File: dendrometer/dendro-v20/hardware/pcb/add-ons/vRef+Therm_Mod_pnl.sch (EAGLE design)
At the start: 8 parts, among them J1 MF-CON-2.54mm-01x03, J2 CON_01X01LUX, J3 MF-CON-2.54mm-01x03, U1 AAT1217-SOT23-6

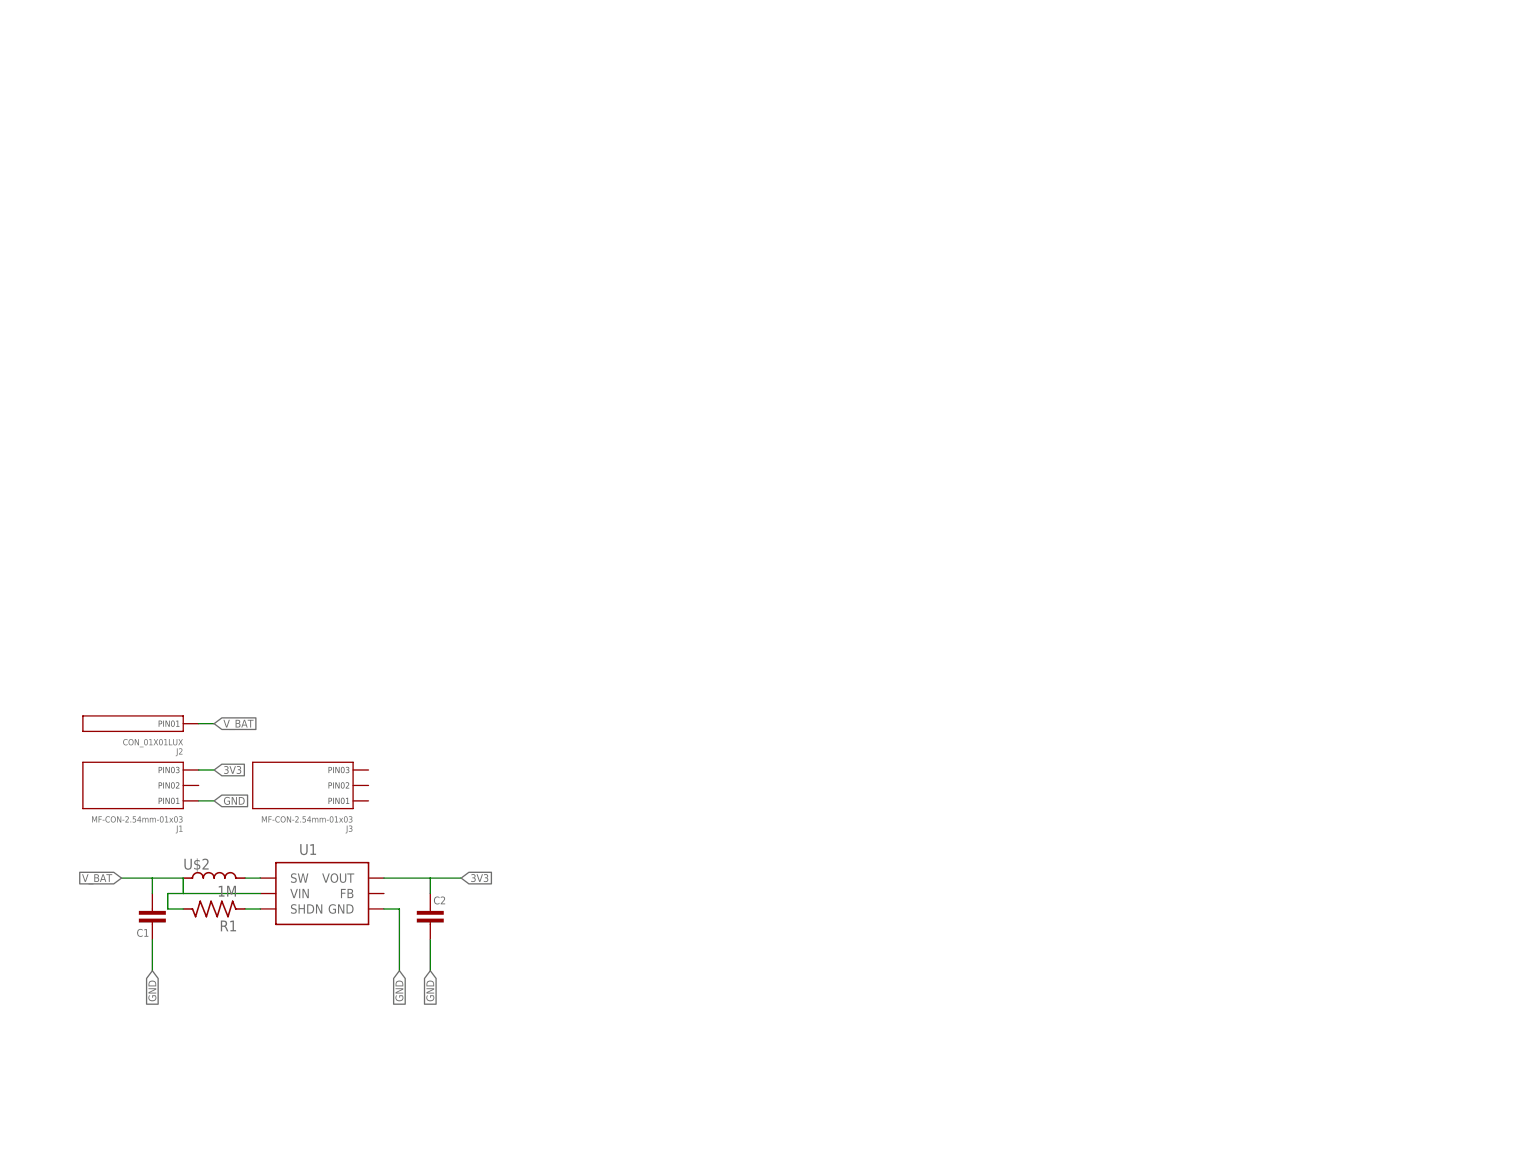
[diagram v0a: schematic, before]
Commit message: making add-on boards for dendro upgrades)
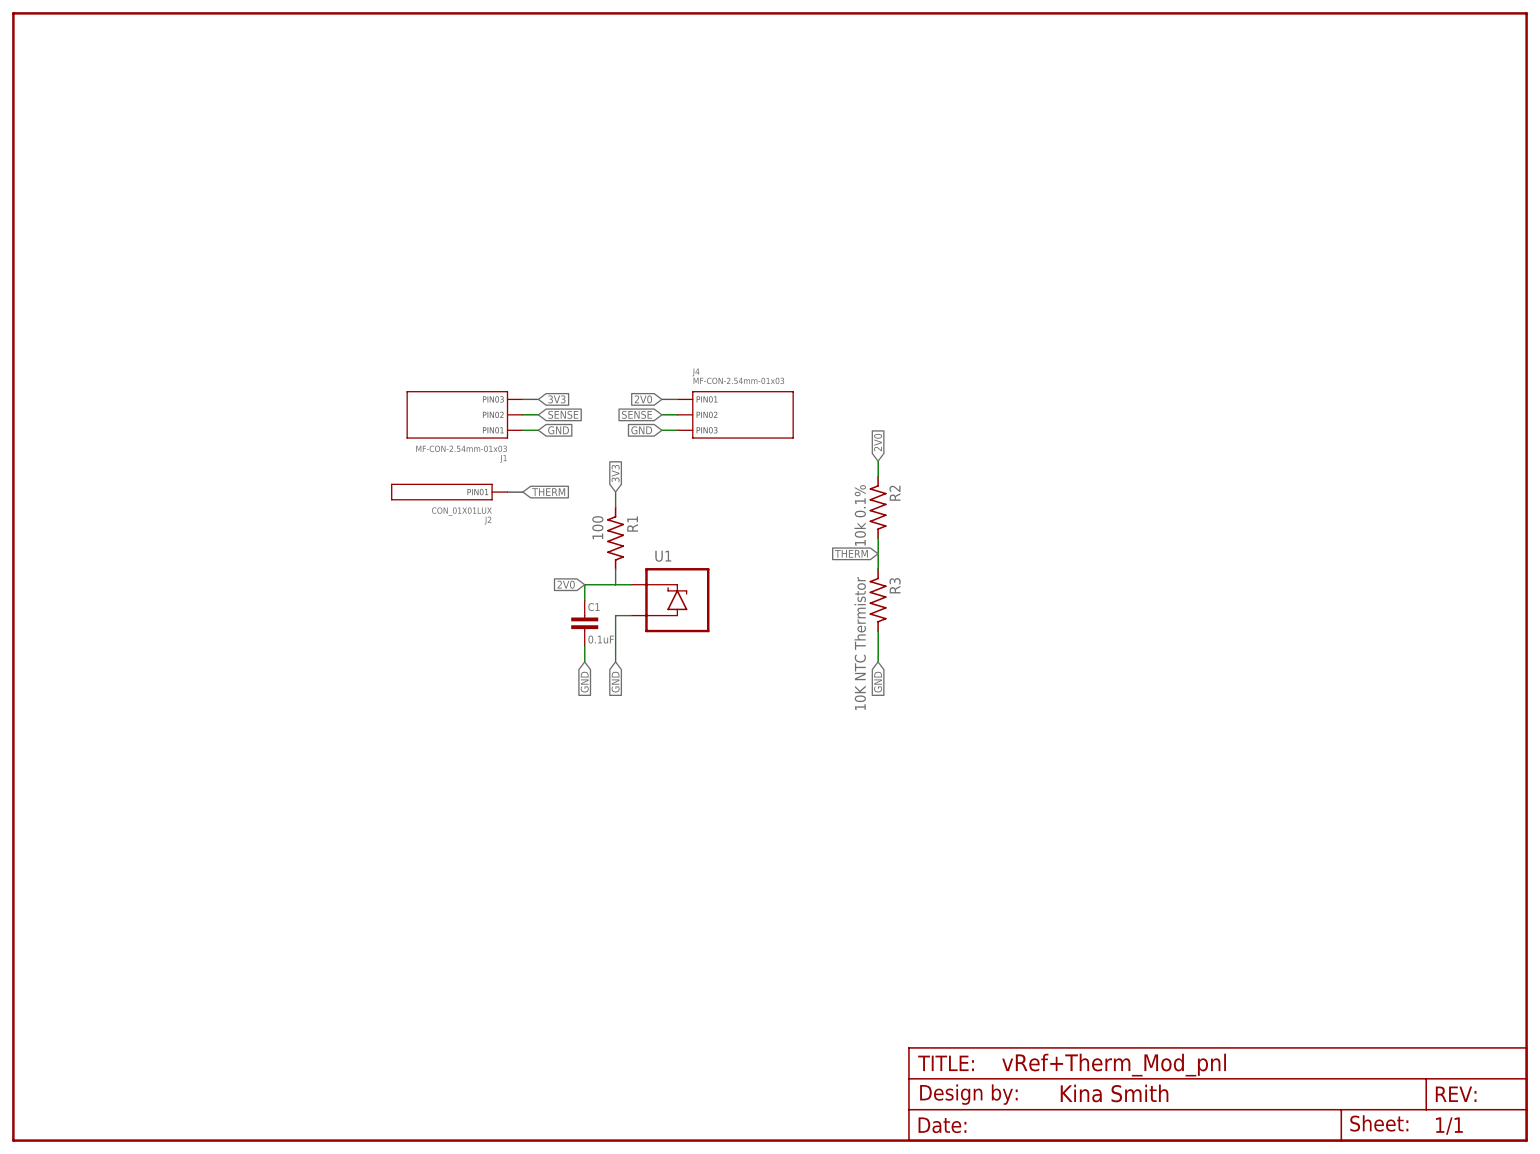
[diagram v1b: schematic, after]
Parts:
- removed C2: (no value), My_Passives:CAPACITOR_NP0603-N
- removed J3: MF-CON-2.54mm-01x03, My_Connectors:CON_01X03_PTH_2.54MM
- removed U$2: (no value), My_Passives:INDUCTOR3030
- added FRAME1: FRAME-LETTERNO_PACKAGE, My_Aesthetics:FRAME-LETTERNO_PACKAGE
- added J4: MF-CON-2.54mm-01x03, My_Connectors:CON_01X03_PTH_2.54MM
- added R2: 10k 0.1%, My_Passives:RESISTOR0603-N
- added R3: 10K NTC Thermistor, My_Passives:RESISTOR0603-N
- C1: value (none) -> 0.1uF
- R1: value 1M -> 100
- U1: value AAT1217-SOT23-6 -> LM4040-SOT-23-3; device My_IC_Power:AAT1217-SOT23-6 -> My_Descrete_Semiconductors:LM4040-SOT-23-3
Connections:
- removed net N$1: U$2.P$2, U1.SW
- removed net N$3: R1.P$1, U1.SHDN
- removed net V_BAT: C1.2, J2.PIN1, R1.P$2, U$2.P$1, U1.VIN
- new net 2V0: C1.1, J4.PIN1, R1.P$2, R2.P$1, U1.C
- new net SENSE: J1.PIN2, J4.PIN2
- new net THERM: J2.PIN1, R2.P$2, R3.P$1
- net 3V3: now also R1.P$1; no longer C2.1, U1.VOUT
- net GND: now also C1.2, J4.PIN3, R3.P$2, U1.A; no longer C1.1, C2.2, U1.GND
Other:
- moved on the sheet: C1, J1, J2, R1
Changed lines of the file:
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@@
 <layer number="154" name="FabDoc2" color="7" fill="1" visible="no" active="yes"/>
 <layer number="155" name="FabDoc3" color="7" fill="1" visible="no" active="yes"/>
-<layer number="188" name="Graphics" color="15" fill="1" visible="no" active="yes"/>
 <layer number="199" name="Contour" color="7" fill="1" visible="no" active="yes"/>
 <layer number="200" name="200bmp" color="1" fill="10" visible="no" active="yes"/>
@@
 </classes>
 <parts>
-<part name="U$2" library="My_Passives" deviceset="INDUCTOR" device="3030"/>
-<part name="R1" library="My_Passives" deviceset="RESISTOR" device="0603-N" value="1M"/>
-<part name="C1" library="My_Passives" deviceset="CAPACITOR_NP" device="0603-N"/>
-<part name="C2" library="My_Passives" deviceset="CAPACITOR_NP" device="0603-N"/>
-<part name="U1" library="My_IC_Power" deviceset="AAT1217" device="-SOT23-6"/>
+<part name="FRAME1" library="My_Aesthetics" deviceset="FRAME-LETTER" device="NO_PACKAGE"/>
+<part name="U1" library="My_Descrete_Semiconductors" deviceset="LM4040" device="-SOT-23-3"/>
+<part name="C1" library="My_Passives" deviceset="CAPACITOR_NP" device="0603-N" value="0.1uF"/>
+<part name="R1" library="My_Passives" deviceset="RESISTOR" device="0603-N" value="100"/>
+<part name="R2" library="My_Passives" deviceset="RESISTOR" device="0603-N" value="10k 0.1%"/>
+<part name="R3" library="My_Passives" deviceset="RESISTOR" device="0603-N" value="10K NTC Thermistor"/>
 <part name="J1" library="My_Connectors" deviceset="CON_01X03" device="_PTH_2.54MM" value="MF-CON-2.54mm-01x03"/>
 <part name="J2" library="My_Connectors" deviceset="CON_01X01" device="LUX"/>
-<part name="J3" library="My_Connectors" deviceset="CON_01X03" device="_PTH_2.54MM" value="MF-CON-2.54mm-01x03"/>
+<part name="J4" library="My_Connectors" deviceset="CON_01X03" device="_PTH_2.54MM" value="MF-CON-2.54mm-01x03"/>
 </parts>
 <sheets>
@@
 </plain>
 <instances>
-<instance part="U$2" gate="G$1" x="33.02" y="43.18"/>
-<instance part="R1" gate="G$1" x="33.02" y="38.1" rot="R180"/>
-<instance part="C1" gate="G$1" x="22.86" y="35.56" rot="R180"/>
-<instance part="C2" gate="G$1" x="68.58" y="38.1"/>
-<instance part="U1" gate="G$1" x="50.8" y="40.64"/>
-<instance part="J1" gate="G$1" x="27.94" y="55.88" rot="R180"/>
-<instance part="J2" gate="G$1" x="27.94" y="68.58" rot="R180"/>
-<instance part="J3" gate="G$1" x="55.88" y="55.88" rot="R180"/>
+<instance part="FRAME1" gate="G$1" x="0" y="0"/>
+<instance part="FRAME1" gate="V" x="147.32" y="0"/>
+<instance part="U1" gate="G$1" x="109.22" y="88.9"/>
+<instance part="C1" gate="G$1" x="93.98" y="86.36"/>
+<instance part="R1" gate="G$1" x="99.06" y="99.06" rot="R270"/>
+<instance part="R2" gate="G$1" x="142.24" y="104.14" rot="R270"/>
+<instance part="R3" gate="G$1" x="142.24" y="88.9" rot="R270"/>
+<instance part="J1" gate="G$1" x="81.28" y="116.84" rot="R180"/>
+<instance part="J2" gate="G$1" x="78.74" y="106.68" rot="R180"/>
+<instance part="J4" gate="G$1" x="111.76" y="121.92"/>
 </instances>
 <busses>
 </busses>
 <nets>
-<net name="N$1" class="0">
+<net name="3V3" class="0">
 <segment>
-<pinref part="U1" gate="G$1" pin="SW"/>
-<pinref part="U$2" gate="G$1" pin="P$2"/>
-<wire x1="40.64" y1="43.18" x2="38.1" y2="43.18" width="0.1524" layer="91"/>
+<pinref part="J1" gate="G$1" pin="PIN3"/>
+<wire x1="83.82" y1="121.92" x2="86.36" y2="121.92" width="0.1524" layer="91"/>
+<label x="86.36" y="121.92" size="1.27" layer="95" xref="yes"/>
 </segment>
-</net>
-<net name="N$3" class="0">
 <segment>
-<pinref part="U1" gate="G$1" pin="SHDN"/>
 <pinref part="R1" gate="G$1" pin="P$1"/>
-<wire x1="40.64" y1="38.1" x2="38.1" y2="38.1" width="0.1524" layer="91"/>
+<wire x1="99.06" y1="104.14" x2="99.06" y2="106.68" width="0.1524" layer="91"/>
+<label x="99.06" y="106.68" size="1.27" layer="95" rot="R90" xref="yes"/>
 </segment>
 </net>
 <net name="GND" class="0">
 <segment>
-<pinref part="C1" gate="G$1" pin="1"/>
-<wire x1="22.86" y1="33.02" x2="22.86" y2="27.94" width="0.1524" layer="91"/>
-<label x="22.86" y="27.94" size="1.27" layer="95" rot="R270" xref="yes"/>
+<pinref part="J1" gate="G$1" pin="PIN1"/>
+<wire x1="83.82" y1="116.84" x2="86.36" y2="116.84" width="0.1524" layer="91"/>
+<label x="86.36" y="116.84" size="1.27" layer="95" xref="yes"/>
 </segment>
 <segment>
-<pinref part="U1" gate="G$1" pin="GND"/>
-<wire x1="60.96" y1="38.1" x2="63.5" y2="38.1" width="0.1524" layer="91"/>
-<wire x1="63.5" y1="38.1" x2="63.5" y2="27.94" width="0.1524" layer="91"/>
-<label x="63.5" y="27.94" size="1.27" layer="95" rot="R270" xref="yes"/>
+<pinref part="J4" gate="G$1" pin="PIN3"/>
+<wire x1="109.22" y1="116.84" x2="106.68" y2="116.84" width="0.1524" layer="91"/>
+<label x="106.68" y="116.84" size="1.27" layer="95" rot="R180" xref="yes"/>
 </segment>
 <segment>
-<pinref part="C2" gate="G$1" pin="2"/>
-<wire x1="68.58" y1="33.02" x2="68.58" y2="27.94" width="0.1524" layer="91"/>
-<label x="68.58" y="27.94" size="1.27" layer="95" rot="R270" xref="yes"/>
+<pinref part="C1" gate="G$1" pin="2"/>
+<wire x1="93.98" y1="81.28" x2="93.98" y2="78.74" width="0.1524" layer="91"/>
+<label x="93.98" y="78.74" size="1.27" layer="95" rot="R270" xref="yes"/>
 </segment>
 <segment>
-<pinref part="J1" gate="G$1" pin="PIN1"/>
-<wire x1="30.48" y1="55.88" x2="33.02" y2="55.88" width="0.1524" layer="91"/>
-<label x="33.02" y="55.88" size="1.27" layer="95" xref="yes"/>
+<pinref part="U1" gate="G$1" pin="A"/>
+<wire x1="101.6" y1="86.36" x2="99.06" y2="86.36" width="0.1524" layer="91"/>
+<wire x1="99.06" y1="86.36" x2="99.06" y2="78.74" width="0.1524" layer="91"/>
+<label x="99.06" y="78.74" size="1.27" layer="95" rot="R270" xref="yes"/>
+</segment>
+<segment>
+<pinref part="R3" gate="G$1" pin="P$2"/>
+<wire x1="142.24" y1="83.82" x2="142.24" y2="78.74" width="0.1524" layer="91"/>
+<label x="142.24" y="78.74" size="1.27" layer="95" rot="R270" xref="yes"/>
 </segment>
 </net>
-<net name="3V3" class="0">
+<net name="SENSE" class="0">
 <segment>
-<pinref part="U1" gate="G$1" pin="VOUT"/>
-<wire x1="60.96" y1="43.18" x2="68.58" y2="43.18" width="0.1524" layer="91"/>
-<pinref part="C2" gate="G$1" pin="1"/>
-<wire x1="68.58" y1="43.18" x2="73.66" y2="43.18" width="0.1524" layer="91"/>
-<wire x1="68.58" y1="40.64" x2="68.58" y2="43.18" width="0.1524" layer="91"/>
-<label x="73.66" y="43.18" size="1.27" layer="95" xref="yes"/>
+<pinref part="J4" gate="G$1" pin="PIN2"/>
+<wire x1="109.22" y1="119.38" x2="106.68" y2="119.38" width="0.1524" layer="91"/>
+<label x="106.68" y="119.38" size="1.27" layer="95" rot="R180" xref="yes"/>
 </segment>
 <segment>
-<pinref part="J1" gate="G$1" pin="PIN3"/>
-<wire x1="30.48" y1="60.96" x2="33.02" y2="60.96" width="0.1524" layer="91"/>
-<label x="33.02" y="60.96" size="1.27" layer="95" xref="yes"/>
+<pinref part="J1" gate="G$1" pin="PIN2"/>
+<wire x1="83.82" y1="119.38" x2="86.36" y2="119.38" width="0.1524" layer="91"/>
+<label x="86.36" y="119.38" size="1.27" layer="95" xref="yes"/>
 </segment>
 </net>
-<net name="V_BAT" class="0">
+<net name="THERM" class="0">
 <segment>
 <pinref part="J2" gate="G$1" pin="PIN1"/>
-<wire x1="30.48" y1="68.58" x2="33.02" y2="68.58" width="0.1524" layer="91"/>
-<label x="33.02" y="68.58" size="1.27" layer="95" xref="yes"/>
+<wire x1="81.28" y1="106.68" x2="83.82" y2="106.68" width="0.1524" layer="91"/>
+<label x="83.82" y="106.68" size="1.27" layer="95" xref="yes"/>
 </segment>
 <segment>
-<pinref part="U$2" gate="G$1" pin="P$1"/>
-<wire x1="27.94" y1="43.18" x2="27.94" y2="40.64" width="0.1524" layer="91"/>
-<pinref part="U1" gate="G$1" pin="VIN"/>
-<wire x1="27.94" y1="40.64" x2="40.64" y2="40.64" width="0.1524" layer="91"/>
-<pinref part="R1" gate="G$1" pin="P$2"/>
-<wire x1="27.94" y1="38.1" x2="25.4" y2="38.1" width="0.1524" layer="91"/>
-<wire x1="25.4" y1="38.1" x2="25.4" y2="40.64" width="0.1524" layer="91"/>
-<wire x1="25.4" y1="40.64" x2="27.94" y2="40.64" width="0.1524" layer="91"/>
-<wire x1="27.94" y1="43.18" x2="22.86" y2="43.18" width="0.1524" layer="91"/>
-<pinref part="C1" gate="G$1" pin="2"/>
-<wire x1="22.86" y1="43.18" x2="17.78" y2="43.18" width="0.1524" layer="91"/>
-<wire x1="22.86" y1="40.64" x2="22.86" y2="43.18" width="0.1524" layer="91"/>
-<label x="17.78" y="43.18" size="1.27" layer="95" rot="R180" xref="yes"/>
+<pinref part="R2" gate="G$1" pin="P$2"/>
+<pinref part="R3" gate="G$1" pin="P$1"/>
+<wire x1="142.24" y1="99.06" x2="142.24" y2="93.98" width="0.1524" layer="91"/>
+<label x="142.24" y="96.52" size="1.27" layer="95" rot="R180" xref="yes"/>
 </segment>
 </net>
+<net name="2V0" class="0">
+<segment>
+<pinref part="R1" gate="G$1" pin="P$2"/>
+<wire x1="99.06" y1="93.98" x2="99.06" y2="91.44" width="0.1524" layer="91"/>
+<pinref part="U1" gate="G$1" pin="C"/>
+<wire x1="99.06" y1="91.44" x2="101.6" y2="91.44" width="0.1524" layer="91"/>
+<wire x1="99.06" y1="91.44" x2="93.98" y2="91.44" width="0.1524" layer="91"/>
+<pinref part="C1" gate="G$1" pin="1"/>
+<wire x1="93.98" y1="91.44" x2="93.98" y2="88.9" width="0.1524" layer="91"/>
+<label x="93.98" y="91.44" size="1.27" layer="95" rot="R180" xref="yes"/>
+</segment>
+<segment>
+<pinref part="R2" gate="G$1" pin="P$1"/>
+<wire x1="142.24" y1="109.22" x2="142.24" y2="111.76" width="0.1524" layer="91"/>
+<label x="142.24" y="111.76" size="1.27" layer="95" rot="R90" xref="yes"/>
+</segment>
+<segment>
+<pinref part="J4" gate="G$1" pin="PIN1"/>
+<wire x1="109.22" y1="121.92" x2="106.68" y2="121.92" width="0.1524" layer="91"/>
+<label x="106.68" y="121.92" size="1.27" layer="95" rot="R180" xref="yes"/>
+</segment>
+</net>
